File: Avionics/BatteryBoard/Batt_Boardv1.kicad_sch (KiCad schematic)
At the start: 42 parts, among them J1 Conn_02x26_Odd_Even, J2 Conn_02x26_Odd_Even, Q1 IRF7458, Q2 IRF7458, U2 BQ29200DRBR, U3 TLA2024IRUGR, U4 LM35-LP, U5 LM35-LP, U6 LM35-LP, U7 LM35-LP

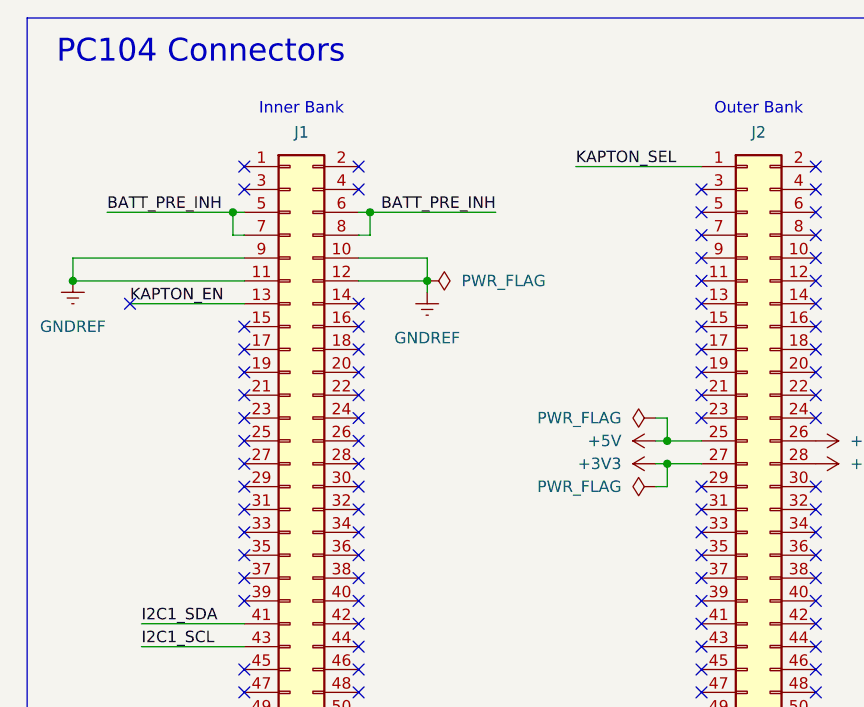
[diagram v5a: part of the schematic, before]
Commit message: batt_brd: discrete heater control has own 5v ldo
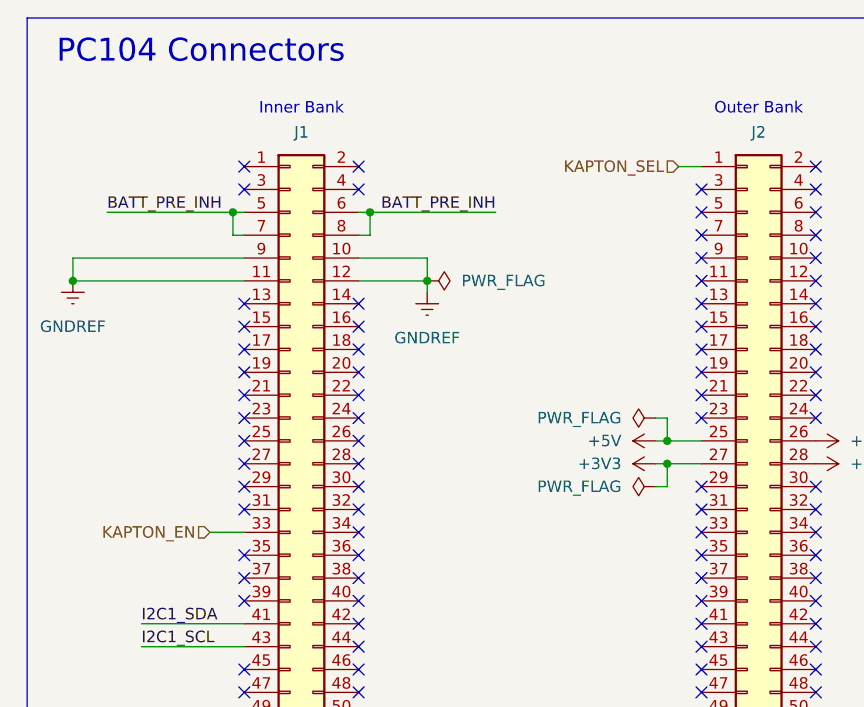
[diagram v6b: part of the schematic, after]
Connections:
- net KAPTON_EN: now also J1.33 (Pin_33); no longer J1.13 (Pin_13)
- no-connect marks 94 -> 93
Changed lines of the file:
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@@
-	)
-	(no_connect
-		(at 38.1 71.12)
 	)
 	(no_connect
@@
 	)
 	(no_connect
-		(at 25.4 45.72)
+		(at 38.1 45.72)
 	)
 	(no_connect
@@
 	(wire
 		(pts
-			(xy 25.4 45.72) (xy 38.1 45.72)
-		)
-		(stroke
-			(width 0)
-			(type default)
-		)
-	)
-	(wire
-		(pts
 			(xy 261.62 26.67) (xy 275.59 26.67)
 		)
@@
 	(wire
 		(pts
+			(xy 86.36 30.48) (xy 88.9 30.48)
+		)
+		(stroke
+			(width 0)
+			(type default)
+		)
+	)
+	(wire
+		(pts
 			(xy 215.9 93.98) (xy 212.09 93.98)
 		)
@@
 	(wire
 		(pts
+			(xy 34.29 71.12) (xy 38.1 71.12)
+		)
+		(stroke
+			(width 0)
+			(type default)
+		)
+	)
+	(wire
+		(pts
 			(xy 261.62 39.37) (xy 261.62 52.07)
 		)
@@
 		(pts
 			(xy 229.87 157.48) (xy 241.3 157.48)
-		)
-		(stroke
-			(width 0)
-			(type default)
-		)
-	)
-	(wire
-		(pts
-			(xy 74.93 30.48) (xy 88.9 30.48)
 		)
 		(stroke
@@
 		)
 	)
-	(label "KAPTON_SEL"
-		(at 74.93 30.48 0)
-		(effects
-			(font
-				(size 1.27 1.27)
-			)
-			(justify left bottom)
-		)
-	)
 	(label "I2C1_SDA"
 		(at 232.41 123.19 270)
@@
 		)
 	)
-	(label "KAPTON_EN"
-		(at 25.4 45.72 0)
-		(effects
-			(font
-				(size 1.27 1.27)
-			)
-			(justify left bottom)
-		)
-	)
 	(label "B-"
 		(at 135.89 64.77 270)
@@
 		)
 	)
+	(hierarchical_label "KAPTON_SEL"
+		(shape input)
+		(at 86.36 30.48 180)
+		(effects
+			(font
+				(size 1.27 1.27)
+			)
+			(justify right)
+		)
+	)
+	(hierarchical_label "KAPTON_EN"
+		(shape input)
+		(at 34.29 71.12 180)
+		(effects
+			(font
+				(size 1.27 1.27)
+			)
+			(justify right)
+		)
+	)

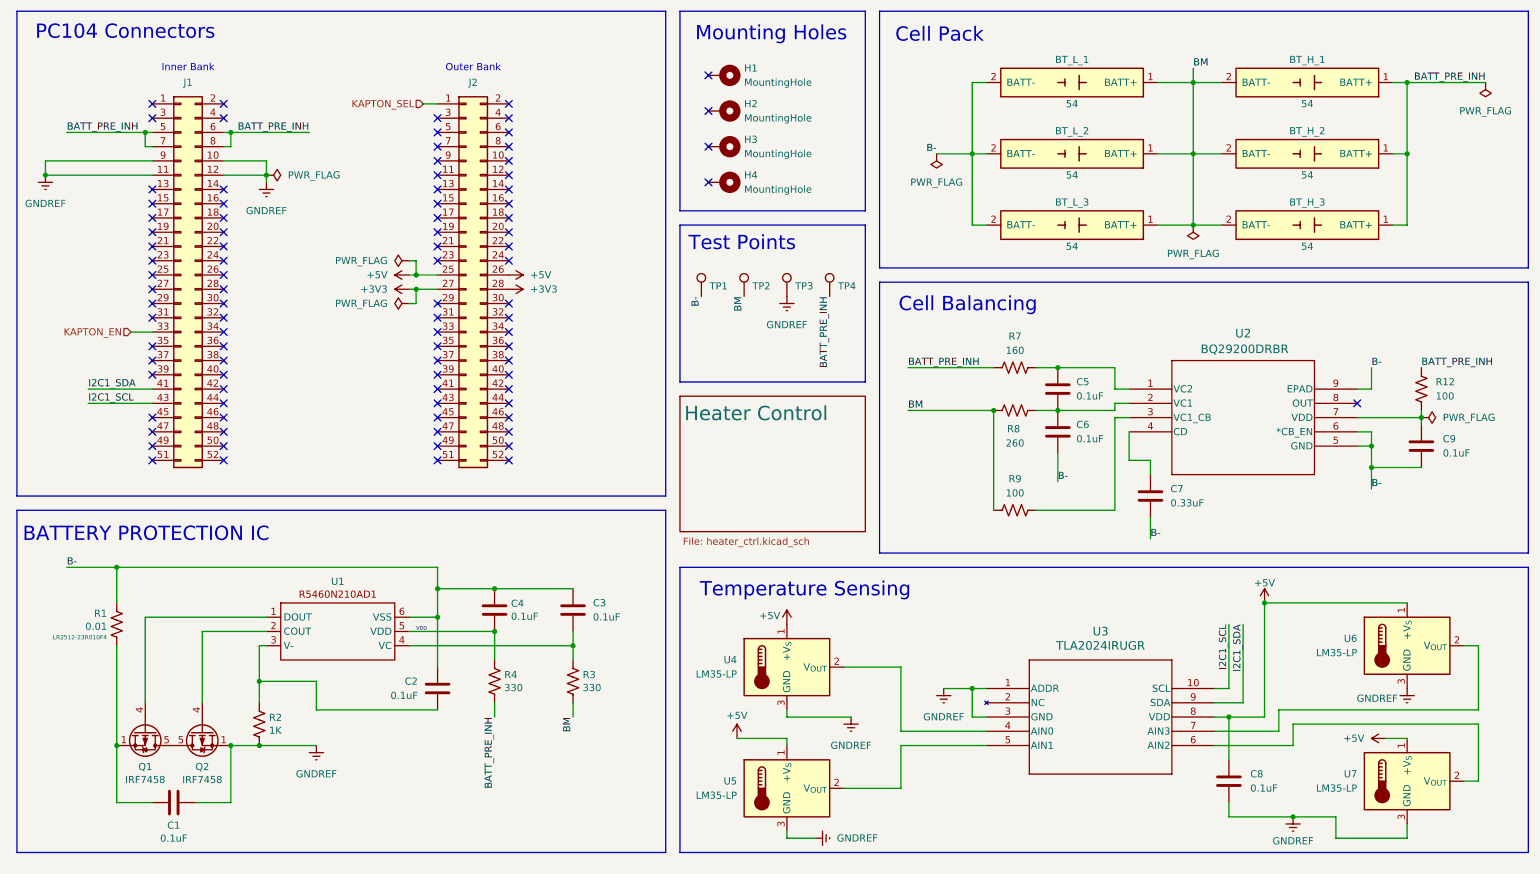
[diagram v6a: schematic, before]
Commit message: batt_brd: prettify
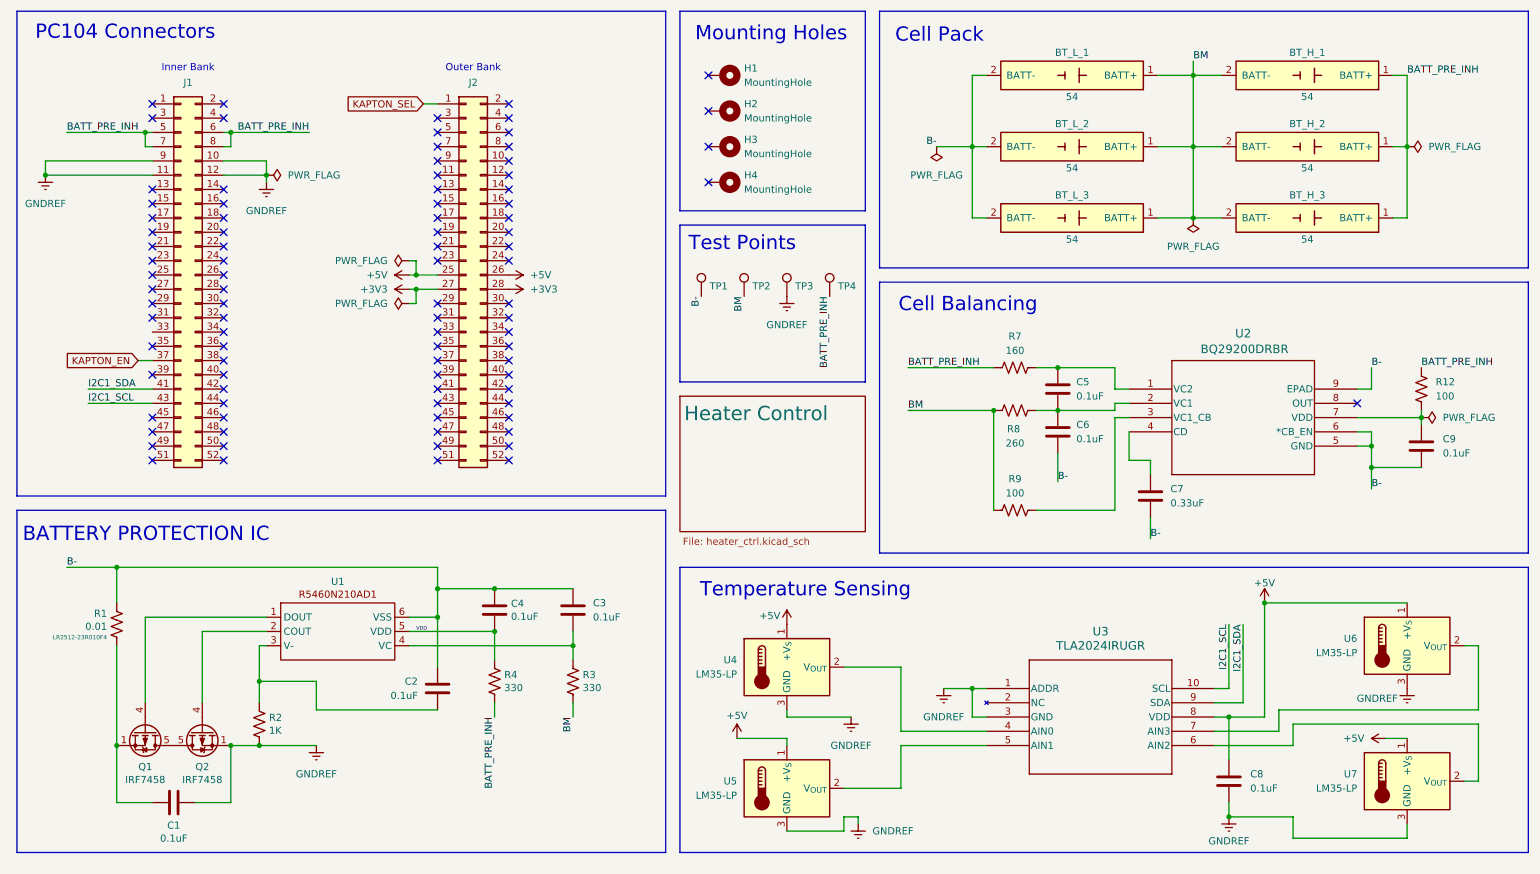
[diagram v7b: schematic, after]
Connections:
- net KAPTON_EN: now also J1.37 (Pin_37); no longer J1.33 (Pin_33)
- no-connect marks 93 -> 92
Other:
- moved on the sheet: BT_H_1, BT_H_2, BT_H_3, BT_L_1, BT_L_2, BT_L_3

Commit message: batt_brd: clean up and add most footprints
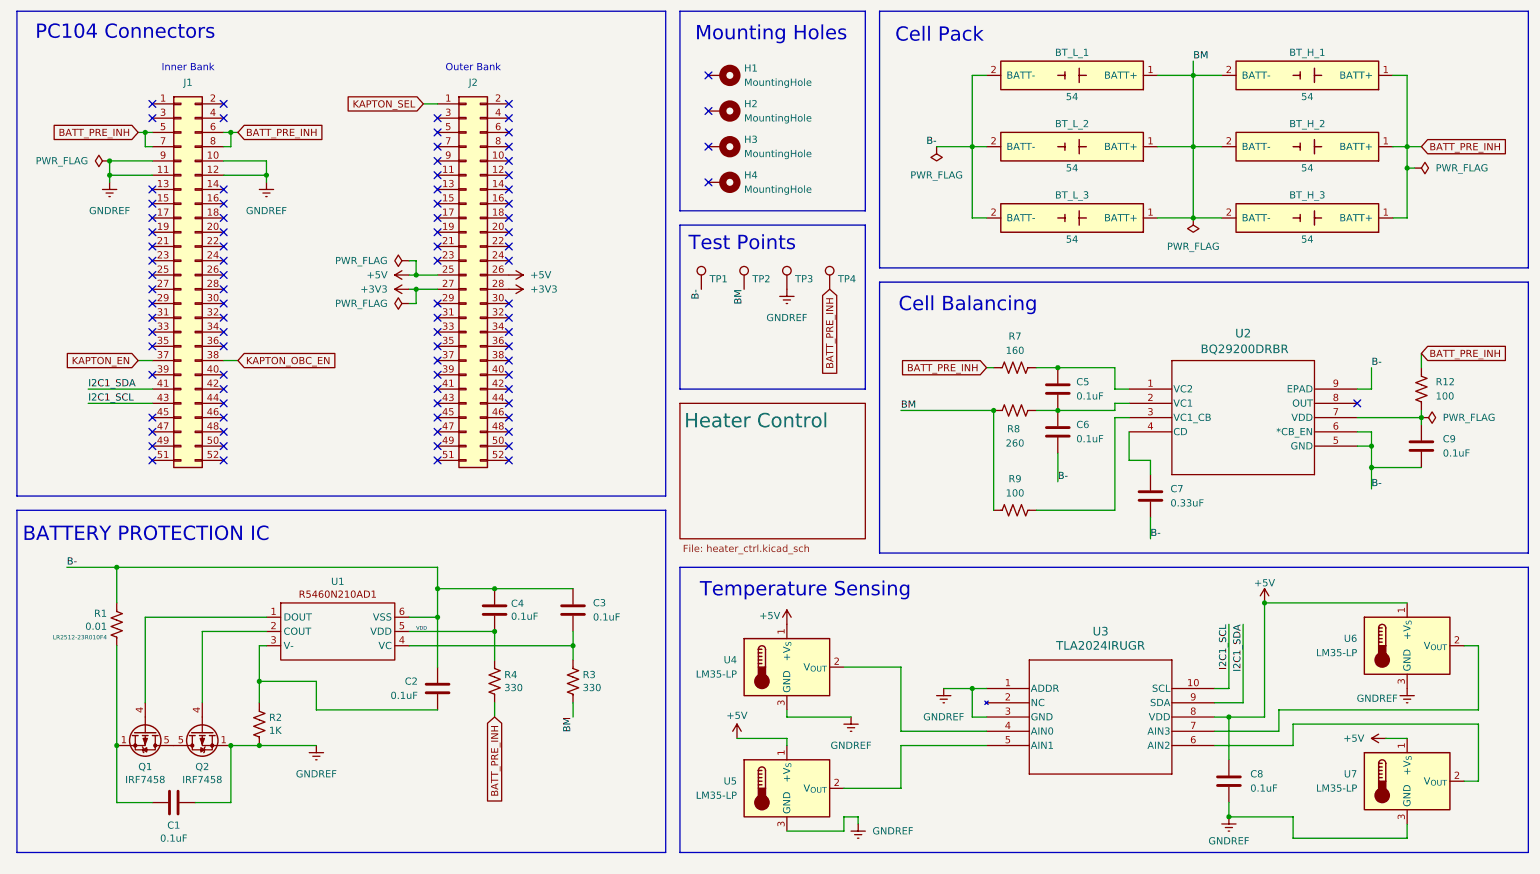
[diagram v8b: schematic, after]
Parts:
- BT_H_1, BT_H_2, BT_H_3, BT_L_1, BT_L_2, BT_L_3: symbol 54 -- Battery clips:54 -> 254TR-18650:254TR-18650
- U2: footprint DRB8_1P6X2P4 -> BattBrdFtPrts:DRB8_1P6X2P4
- U3: footprint RUG10_TEX -> BattBrdFtPrts:RUG10_TEX
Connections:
- net KAPTON_OBC_EN: now reaches J1.38 (Pin_38)
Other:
- moved on the sheet: TP1, TP2, TP3, TP4
